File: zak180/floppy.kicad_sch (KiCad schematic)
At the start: 7 parts, among them J1 Conn_02x17_Odd_Even, U1 82077AA/PC8477, Y1 24 MHz

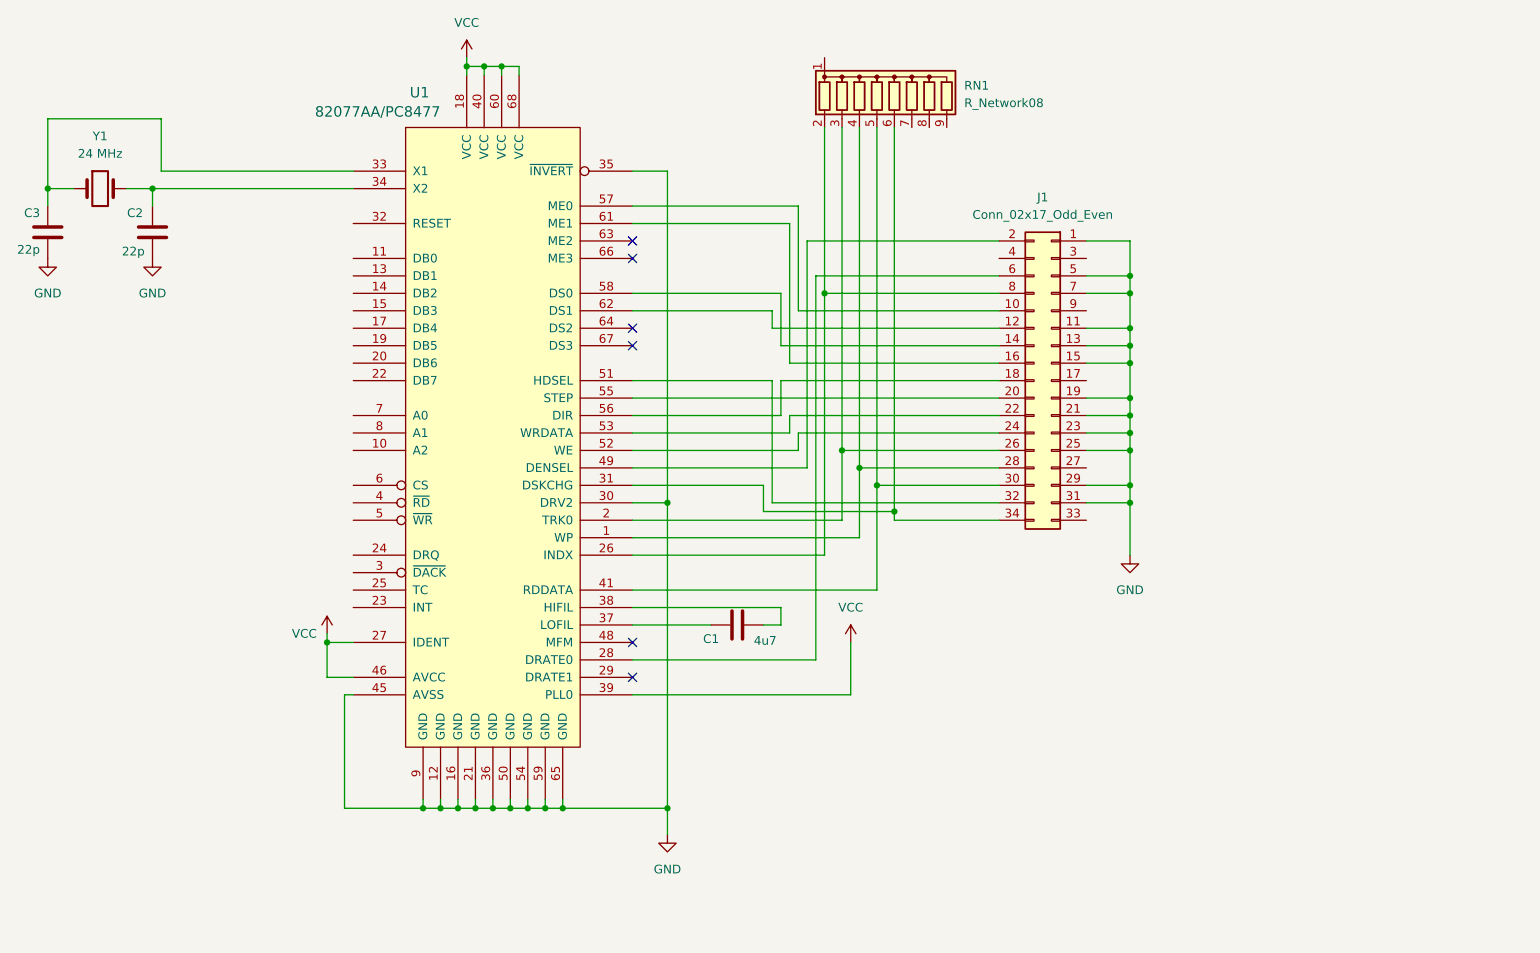
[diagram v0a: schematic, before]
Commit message: HW: Floppy, VGA, PIO and sound
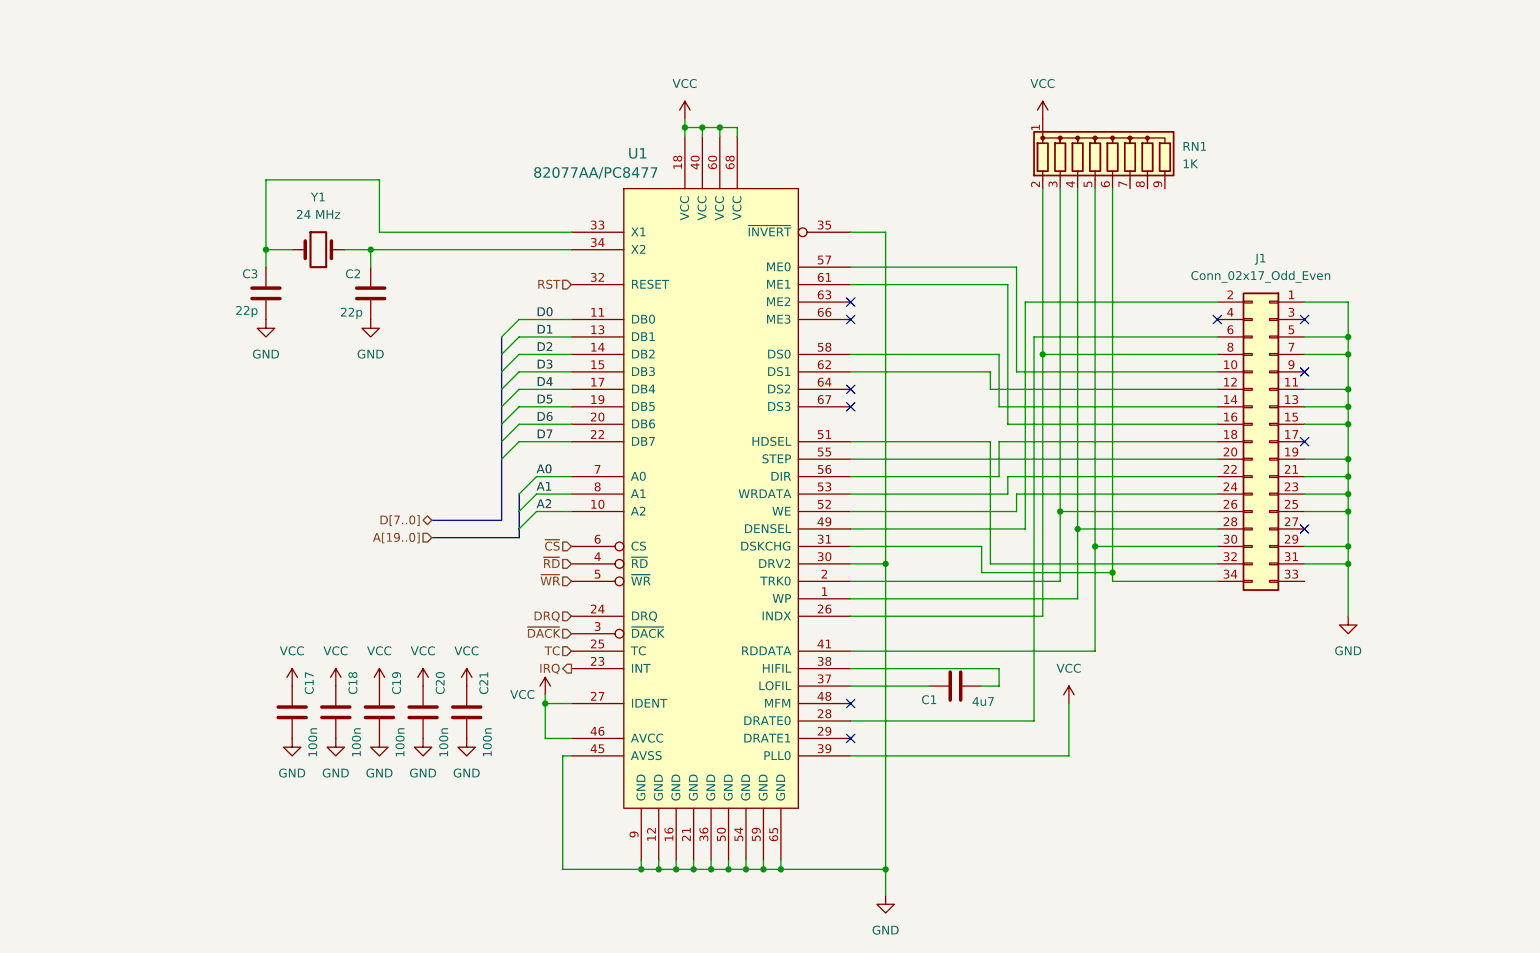
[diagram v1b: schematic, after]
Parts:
- added C17, C18, C19, C20, C21: 100n, Capacitor_THT:C_Disc_D5.0mm_W2.5mm_P2.50mm, symbol Device:C
- RN1: value R_Network08 -> 1K
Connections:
- net GND: now also C17.2, C18.2, C19.2, C20.2, C21.2
- net VCC: now also RN1.1 (common), C17.1, C18.1, C19.1, C20.1, C21.1
- net A2: now reaches U1.10 (A2)
- net D0: now reaches U1.11 (DB0)
- net D1: now reaches U1.13 (DB1)
- net D2: now reaches U1.14 (DB2)
- net D3: now reaches U1.15 (DB3)
- net D4: now reaches U1.17 (DB4)
- net D5: now reaches U1.19 (DB5)
- net D6: now reaches U1.20 (DB6)
- net D7: now reaches U1.22 (DB7)
- net IRQ: now reaches U1.23 (INT)
- net DRQ: now reaches U1.24 (DRQ)
- net TC: now reaches U1.25 (TC)
- net ~{DACK}: now reaches U1.3 (~{DACK})
- net RST: now reaches U1.32 (RESET)
- net ~{RD}: now reaches U1.4 (~{RD})
- net ~{WR}: now reaches U1.5 (~{WR})
- net ~{CS}: now reaches U1.6 (CS)
- net A0: now reaches U1.7 (A0)
- net A1: now reaches U1.8 (A1)
- no-connect marks 6 -> 11
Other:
- moved on the sheet: C1, C2, C3, J1, RN1, U1, Y1

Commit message: HW: Further work on schematic
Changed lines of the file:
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@@
 		)
 	)
-	(hierarchical_label "A[19..0]"
+	(hierarchical_label "A[2..0]"
 		(shape input)
 		(at 86.36 102.87 180)

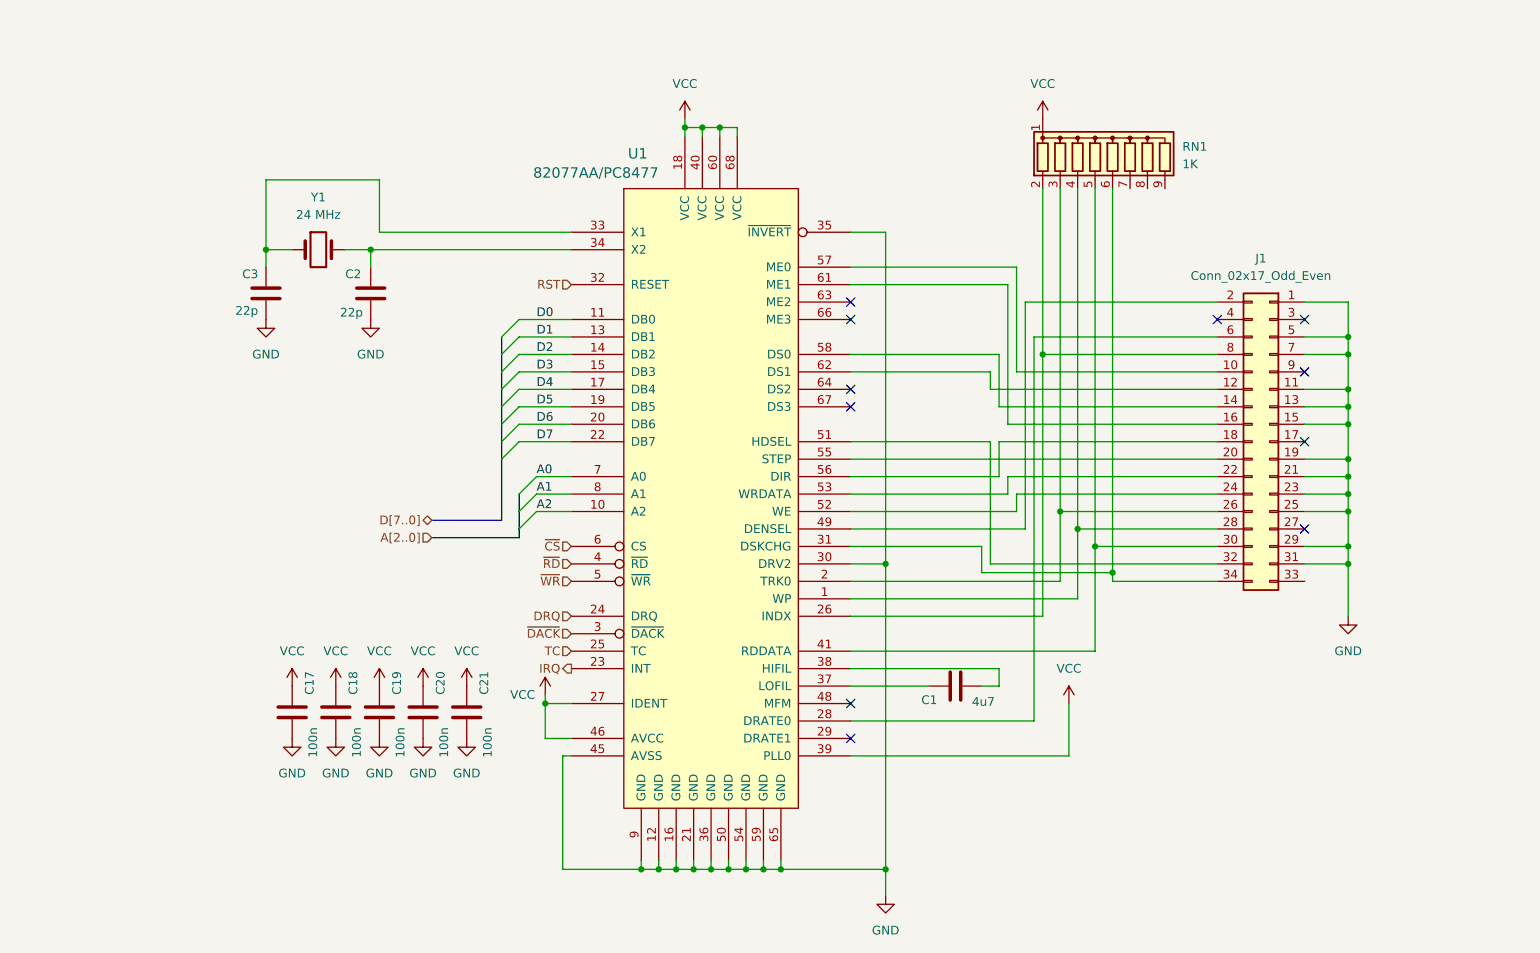
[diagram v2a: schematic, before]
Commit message: HW: Add memory, serial and power
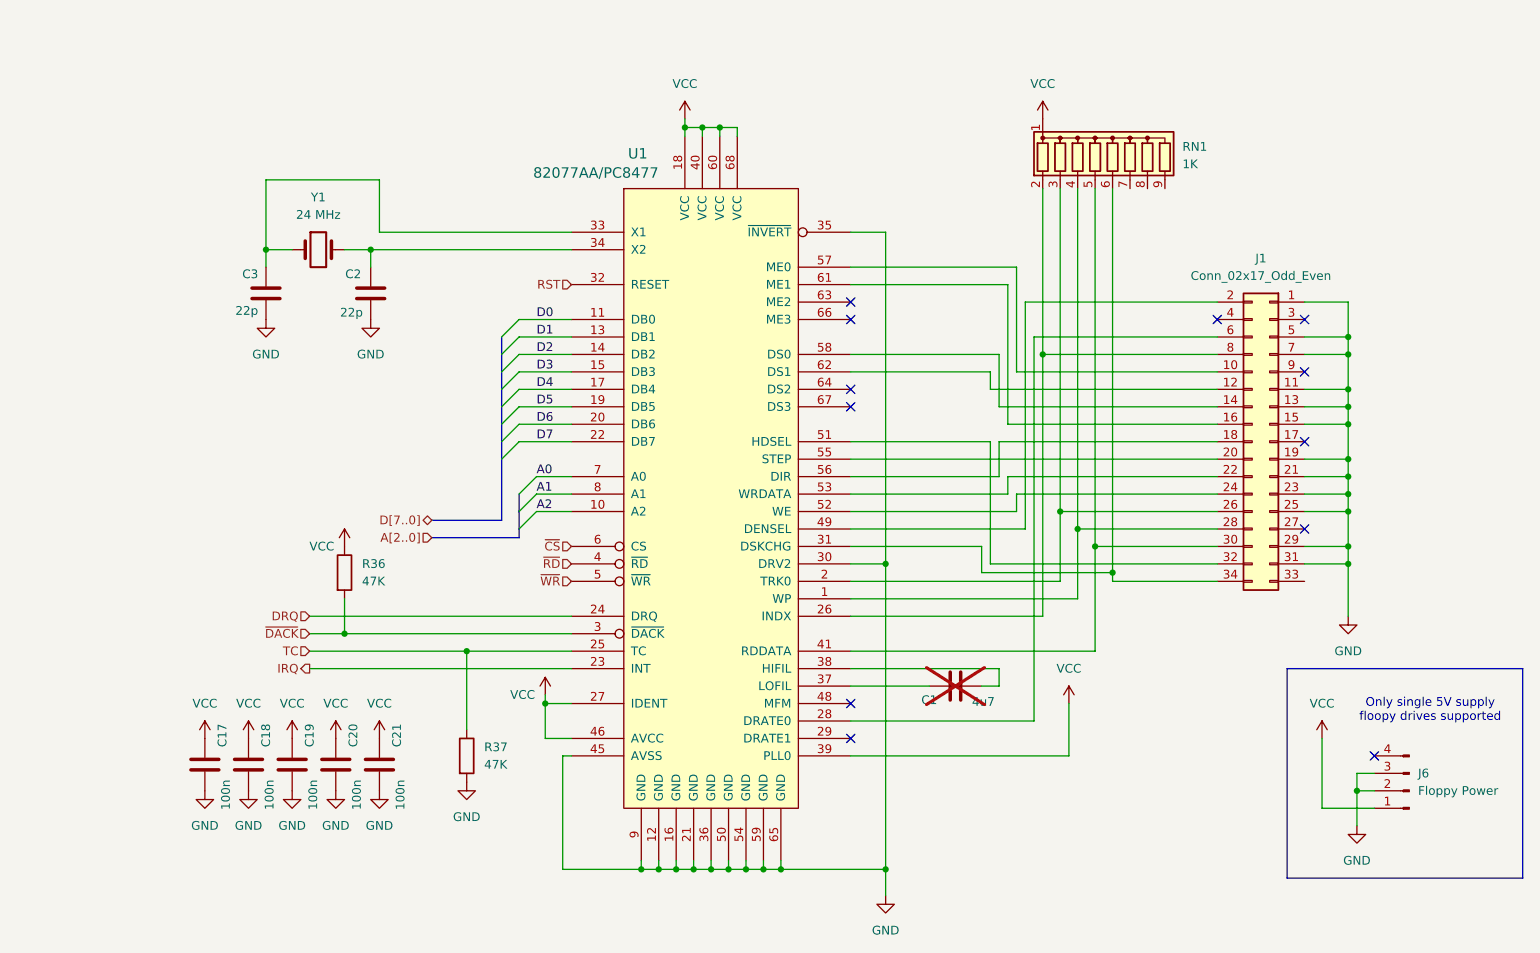
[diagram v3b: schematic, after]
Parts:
- added J6: Floppy Power, Connector_PinHeader_2.54mm:PinHeader_1x04_P2.54mm_Horizontal, symbol Connector:Conn_01x04_Pin
- added R36, R37: 47K, Resistor_THT:R_Axial_DIN0207_L6.3mm_D2.5mm_P7.62mm_Horizontal, symbol Device:R
- C1: now not fitted
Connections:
- net GND: now also J6.2 (Pin_2), J6.3 (Pin_3), R37.2
- net TC: now also R37.1
- net VCC: now also J6.1 (Pin_1), R36.1
- net ~{DACK}: now also R36.2
- no-connect marks 11 -> 12
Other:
- note added: "Only single 5V supply floopy drives supported"
- moved on the sheet: C17, C18, C19, C20, C21

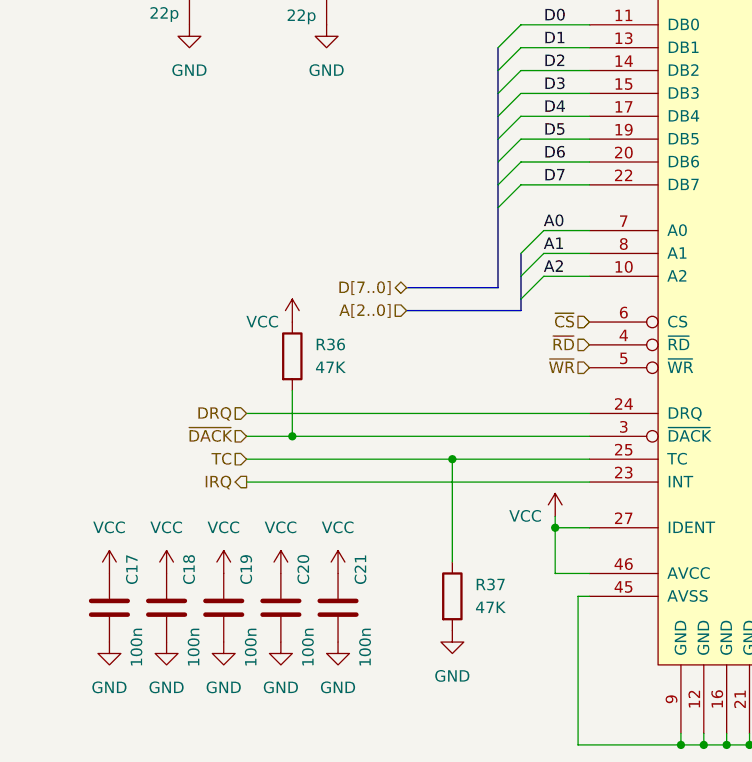
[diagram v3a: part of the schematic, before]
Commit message: HW: Before abandoning DRAM
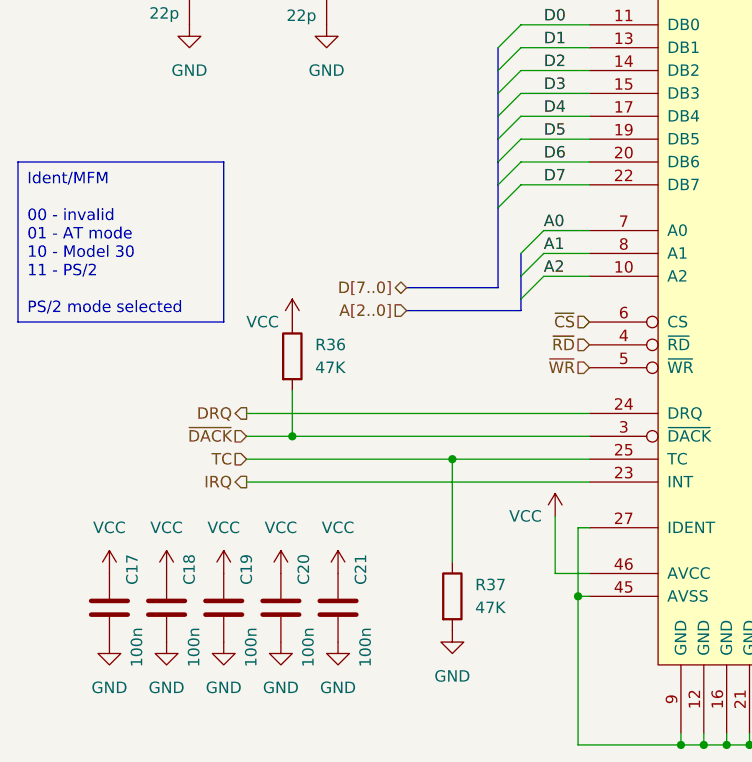
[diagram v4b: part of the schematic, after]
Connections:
- net GND: now also U1.27 (IDENT)
- net VCC: no longer U1.27 (IDENT)
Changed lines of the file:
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@@
-	)
-	(junction
-		(at 102.87 127)
-		(diameter 0)
-		(color 0 0 0 0)
 	)
 	(junction
@@
 	(junction
 		(at 134.62 151.13)
+		(diameter 0)
+		(color 0 0 0 0)
+	)
+	(junction
+		(at 105.41 134.62)
 		(diameter 0)
 		(color 0 0 0 0)
@@
 	(wire
 		(pts
-			(xy 102.87 132.08) (xy 102.87 127)
+			(xy 102.87 125.73) (xy 102.87 132.08)
 		)
 		(stroke
@@
 	(wire
 		(pts
-			(xy 102.87 127) (xy 102.87 125.73)
-		)
-		(stroke
-			(width 0)
-			(type default)
-		)
-	)
-	(wire
-		(pts
 			(xy 77.47 60.96) (xy 106.68 60.96)
 		)
@@
 	(wire
 		(pts
-			(xy 102.87 127) (xy 106.68 127)
-		)
-		(stroke
-			(width 0)
-			(type default)
-		)
-	)
-	(wire
-		(pts
 			(xy 167.64 81.28) (xy 167.64 78.74)
 		)
@@
 	(wire
 		(pts
+			(xy 105.41 134.62) (xy 105.41 127)
+		)
+		(stroke
+			(width 0)
+			(type default)
+		)
+	)
+	(wire
+		(pts
 			(xy 219.71 99.06) (xy 219.71 104.14)
 		)
@@
 		(pts
 			(xy 172.72 68.58) (xy 200.66 68.58)
+		)
+		(stroke
+			(width 0)
+			(type default)
+		)
+	)
+	(wire
+		(pts
+			(xy 105.41 127) (xy 106.68 127)
 		)
 		(stroke
@@
 		(fill
 			(type none)
+		)
+	)
+	(text_box "Ident/MFM\n\n00 - invalid\n01 - AT mode\n10 - Model 30\n11 - PS/2\n\nPS/2 mode selected"
+		(exclude_from_sim no)
+		(at 43.18 86.36 0)
+		(size 22.86 17.78)
+		(stroke
+			(width 0)
+			(type default)
+		)
+		(fill
+			(type none)
+		)
+		(effects
+			(font
+				(size 1.27 1.27)
+			)
+			(justify left top)
 		)
 	)
@@
 	)
 	(hierarchical_label "DRQ"
-		(shape input)
+		(shape output)
 		(at 68.58 114.3 180)
 		(fields_autoplaced yes)

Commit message: HW: Change RAM to static
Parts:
- J1: footprint (none) -> Connector_IDC:IDC-Header_2x17_P2.54mm_Vertical
- U1: footprint Custom KiCad Library:PLCC-68_THT-Socket -> Package_LCC:PLCC-68_THT-Socket
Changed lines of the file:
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@@
 			)
 		)
-		(property "Footprint" ""
+		(property "Footprint" "Connector_IDC:IDC-Header_2x17_P2.54mm_Vertical"
 			(at 208.28 88.9 0)
 			(effects
@@
 			)
 		)
-		(property "Footprint" "Custom KiCad Library:PLCC-68_THT-Socket"
+		(property "Footprint" "Package_LCC:PLCC-68_THT-Socket"
 			(at 127 96.52 0)
 			(effects
